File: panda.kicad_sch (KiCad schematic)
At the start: 14 parts

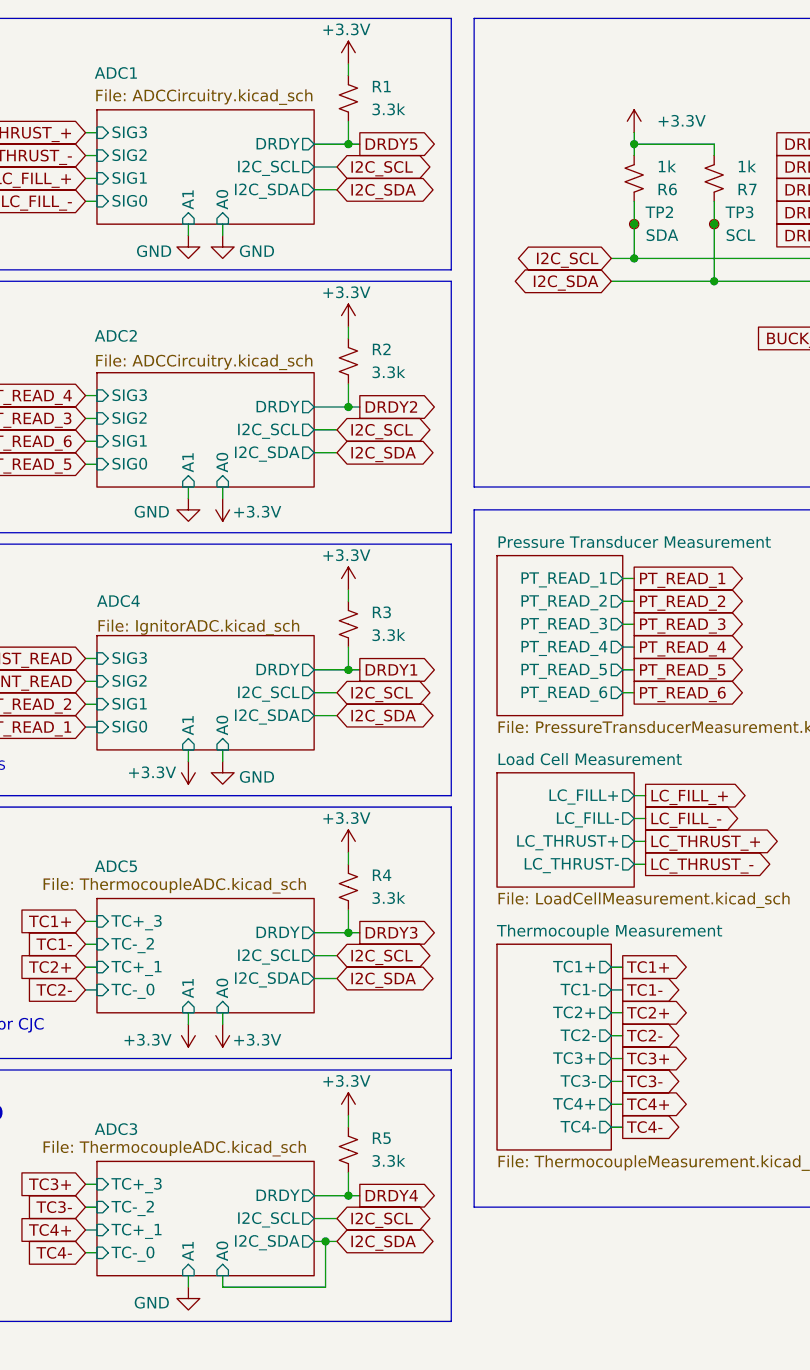
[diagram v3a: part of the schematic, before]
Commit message: fix drdy pin numbering
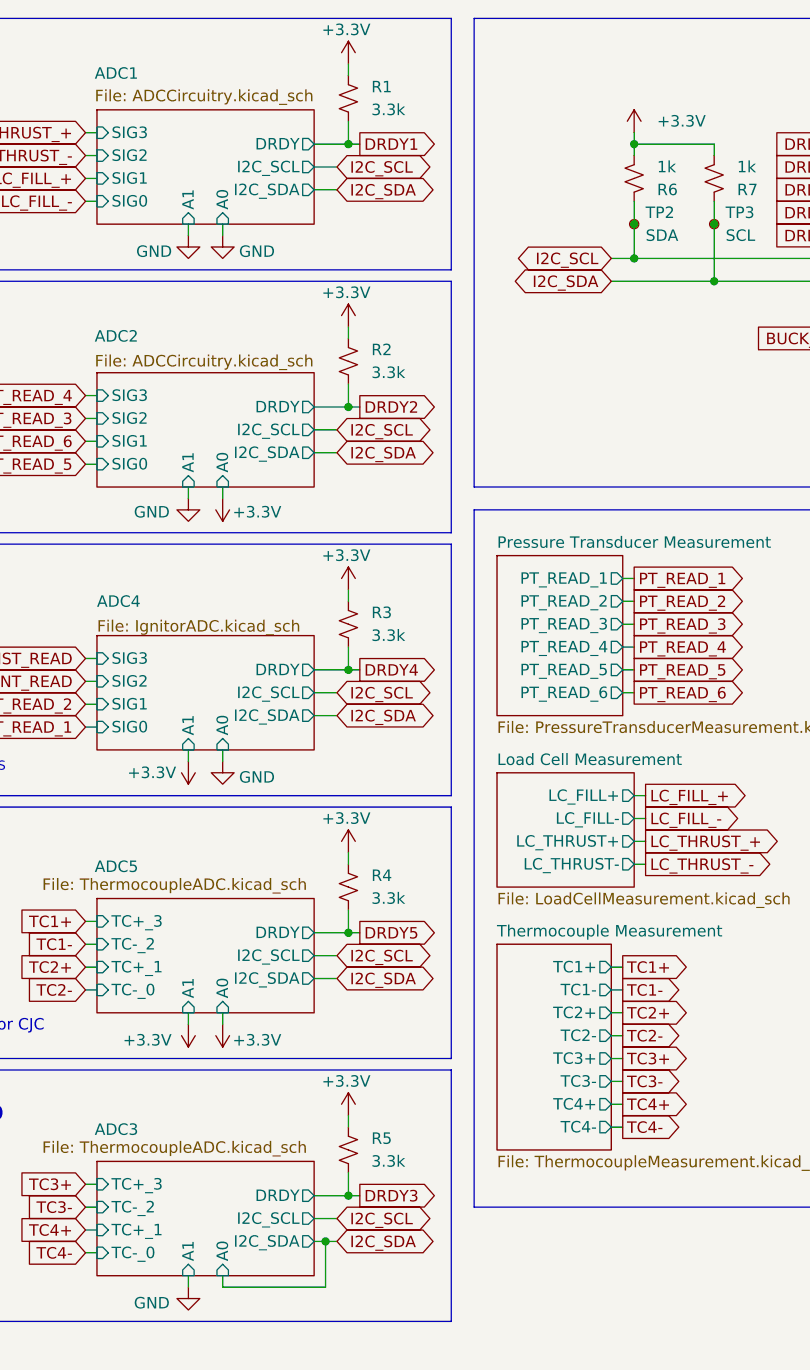
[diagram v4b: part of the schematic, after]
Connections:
- net DRDY1: now also R1.2; no longer R3.2
- net DRDY3: now also R5.2; no longer R4.2
- net DRDY4: now also R3.2; no longer R5.2
- net DRDY5: now also R4.2; no longer R1.2
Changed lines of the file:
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@@
+		)
+	)
+	(global_label "DRDY4"
+		(shape output)
+		(at 77.47 86.36 0)
+		(fields_autoplaced yes)
+		(effects
+			(font
+				(size 1.27 1.27)
+			)
+			(justify left)
+		)
+		(property "Intersheetrefs" "${INTERSHEET_REFS}"
+			(at 86.5633 86.36 0)
+			(effects
+				(font
+					(size 1.27 1.27)
+				)
+				(justify left)
+				(hide yes)
+			)
 		)
 	)
 	(global_label "DRDY1"
-		(shape output)
-		(at 77.47 86.36 0)
-		(fields_autoplaced yes)
-		(effects
-			(font
-				(size 1.27 1.27)
-			)
-			(justify left)
-		)
-		(property "Intersheetrefs" "${INTERSHEET_REFS}"
-			(at 86.5633 86.36 0)
-			(effects
-				(font
-					(size 1.27 1.27)
-				)
-				(justify left)
-				(hide yes)
-			)
-		)
-	)
-	(global_label "DRDY1"
 		(shape input)
 		(at 132.08 27.94 180)
@@
 		)
 	)
-	(global_label "DRDY4"
+	(global_label "DRDY3"
 		(shape output)
 		(at 77.47 144.78 0)
@@
 		)
 	)
-	(global_label "DRDY3"
+	(global_label "DRDY5"
 		(shape output)
 		(at 77.47 115.57 0)
@@
 		)
 	)
-	(global_label "DRDY5"
+	(global_label "DRDY1"
 		(shape output)
 		(at 77.47 27.94 0)
